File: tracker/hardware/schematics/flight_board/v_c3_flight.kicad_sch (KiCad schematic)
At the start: 20 parts, among them J1 Prog_Header, J2 Debug_Header, U1 ESP32-C3-WROOM-02, U2 LR2021F33, U3 MAX-M10S, U4 TPS7A02, U5 BMP280

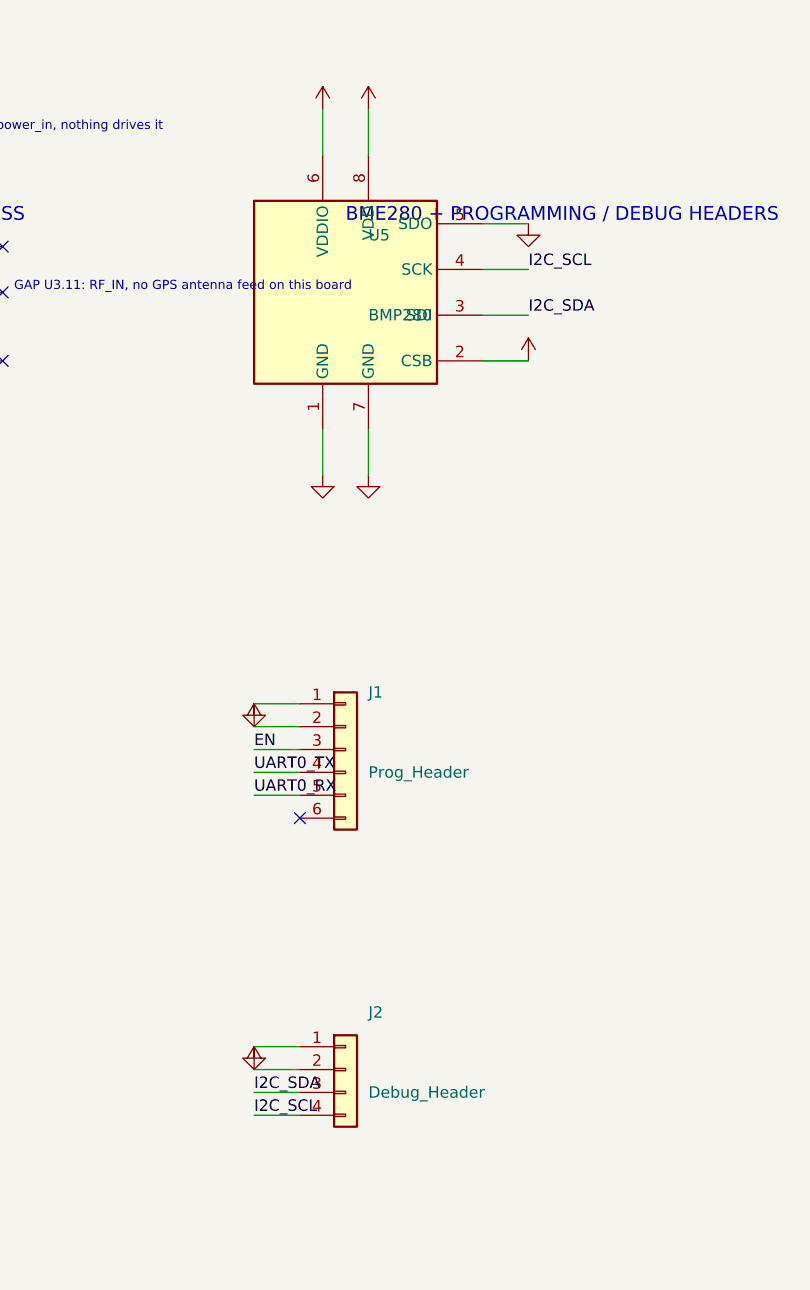
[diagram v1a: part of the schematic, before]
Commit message: M1: align MS5611 design-backing artifacts (BOM, netlist, generator, schematics)
- v8b BOM/position files now list U5 as MS5611 with Package_LGA:LGA-8_3x5mm_P1.25mm
- flight_board netlist, build script, and regenerated schematic now emit Sensor_Pressure:MS5611-01BA
- top-level v_c3_flight.kicad_sch U5 symbol/value/footprint updated to MS5611-01BA
- hub_schematic stale BMP280-only comment fixed

No active design source file still declares BMP280 as the populated part.
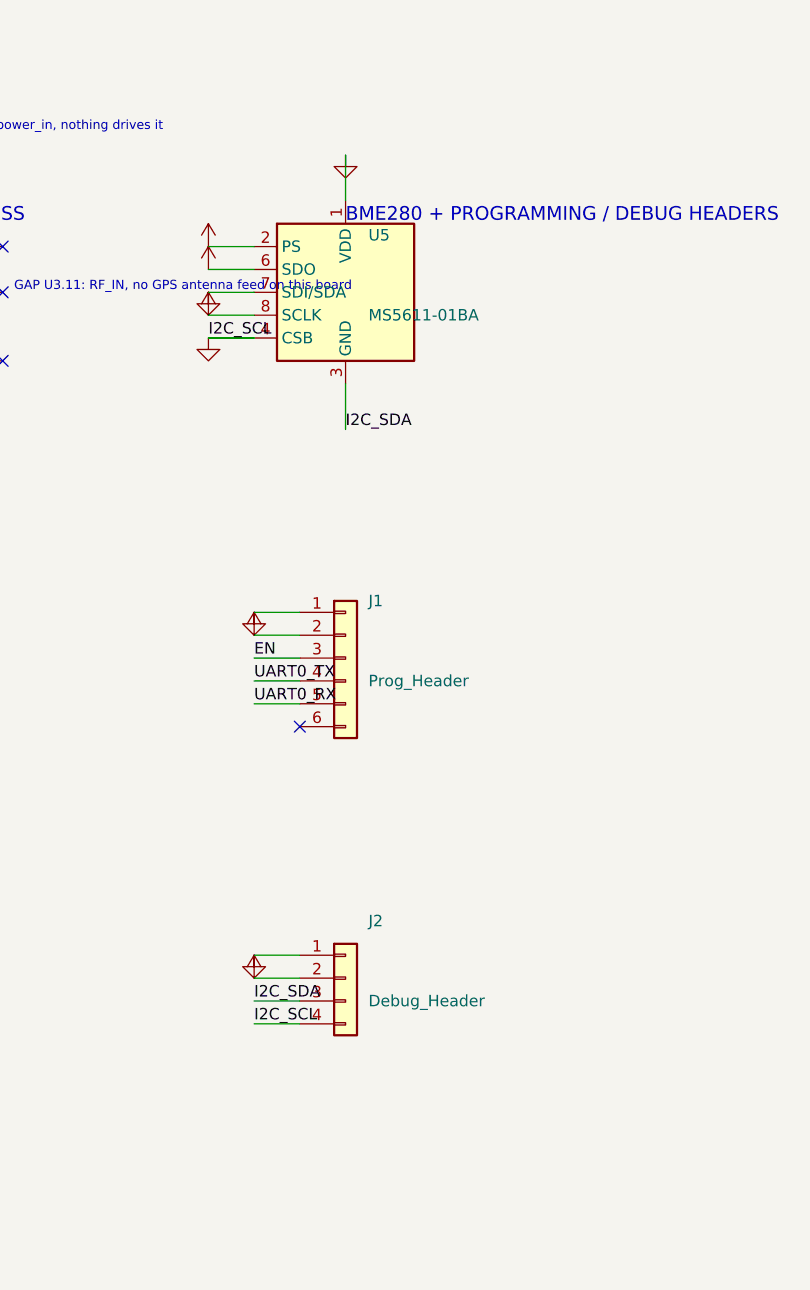
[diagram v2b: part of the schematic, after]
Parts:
- removed U5: BMP280, balloon_flight:Bosch_LGA-8_2.5x2.5mm_P0.65mm_ClockwisePinNumbering, symbol Sensor:BME280
- added U5: MS5611-01BA, Package_LGA:LGA-8_3x5mm_P1.25mm, symbol Sensor_Pressure:MS5611-01BA
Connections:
- net I2C_SCL is gone; now on net GND: J2.4 (Pin_4), U1.8 (IO9)
- net +3V3: now also U5.2 (PS), U5.6 (SDO), U5.8 (SCLK)
- net GND: now also U5.1 (VDD), U5.4 (CSB), U5.5 (CSB), U5.7 (SDI/SDA)
- net I2C_SDA: now also U5.3 (GND)

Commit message: fix(sch): sync flight schematic to v8i board of record (20→28 components)
Re-point build_flight_sch.py at the board of record
v8i_krt_gnss.kicad_pcb (28 footprints, 25 nets) instead of the stale
v_c3_flight_4layer_placed.kicad_pcb (20 footprints).  This brings the
drawing up to the board and closes the GNSS-path gap the drawing itself
documented.

Added 8 components present on the board but missing from the drawing:
  ANT2 (U.FL_GNSS), R_SER (0R), C_SH1/C_SH2 (DNP shunts), MNT1-4 (mounting holes)

GNSS antenna feed now wired:
  ANT2.1 -> GNSS_ANT -> R_SER -> GNSS_RF -> U3.11 (RF_IN)
  C_SH1 shunts GNSS_RF to GND; C_SH2 shunts GNSS_ANT to GND
  The 'no GPS antenna feed on this board' annotation is removed (U3.11
  now has a net, so the gap note no longer fires).

U2 updated to the 18-pin LoRa2021_Castellated footprint (Gen4 module)
with net-derived pin names; floating pads (10/13/16/17) left with
TODO(unverified) annotations (never tie a 2W PA module pin on a guess).

U3.9 (~RESET) and U3.6 (V_BCKP) are now tied to +3V3 by the board itself
(no longer floating).  U3.15 (VIO_SEL) and U3.18 (~SAFEBOOT) remain
floating with TODO(unverified) annotations — the u-blox MAX-M10S
integration manual was not sourced in time to apply the datasheet
tie-off.

U5 remains MS5611-01BA (value/footprint override preserved).  The symbol
is Sensor:BME280 (BMP280 pad numbering matching the board) with the
value/footprint overridden to MS5611-01BA / LGA-8_3x5mm_P1.25mm, fixing
a pin-numbering mismatch that caused ERC errors when mapped to the
Sensor_Pressure:MS5611-01BA symbol directly.

Verification: check_sch_gates.py ALL GATES PASS (0 ERC errors, 1
warning); kicad-cli sch export netlist emits 28 components; net/node
parity with the PCB verified both ways (24 nets, 98 nodes).
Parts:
- removed U5: MS5611-01BA, Package_LGA:LGA-8_3x5mm_P1.25mm, symbol Sensor_Pressure:MS5611-01BA
- added ANT2: U.FL_GNSS, balloon_flight:U.FL_Molex_MCRF_73412-0110_Vertical, symbol Connector:Conn_Coaxial
- added C_SH1, C_SH2: DNP, balloon_flight:C_0402_1005Metric, symbol Device:C
- added MNT1, MNT2, MNT3, MNT4: MountingHole, balloon_flight:MountingHole_2.2mm_M2, symbol Mechanical:MountingHole
- added R_SER: 0R, balloon_flight:R_0402_1005Metric, symbol Device:R
- added U5: MS5611-01BA, Package_LGA:LGA-8_3x5mm_P1.25mm, symbol Sensor:BME280
- U2: value LR2021F33 -> LoRa2021_Gen4; footprint balloon_flight:HOPERF_RFM9XW_SMD -> balloon_flight:LoRa2021_Castellated
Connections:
- net +3V3: now also U2.1 (VCC), U3.6 (V_BCKP), U3.9 (~{RESET}), U5.2 (CSB), U5.6 (VDDIO), U5.8 (VDD); no longer U2.13 (VCC)
- net GND: now also U2.11 (GND), U2.12 (GND), U2.18 (GND), U2.2 (GND), ANT2.2 (Ext), C_SH1.1, C_SH2.1, U5.1 (GND), U5.5 (SDO), U5.7 (GND); no longer J2.4 (Pin_4), U1.8 (IO9), U2.1 (GND), U2.10 (GND)
- net I2C_SDA: now also U5.3 (SDI)
- net LR_BUSY: now also U2.7 (BUSY); no longer U2.12 (BUSY)
- net LR_RST: now also U2.14 (RESET); no longer U2.6 (RESET)
- net SPI_MISO: now also U2.3 (MISO); no longer U2.2 (MISO)
- net SPI_MOSI: now also U2.4 (MOSI); no longer U2.3 (MOSI)
- net SPI_NSS: now also U2.6 (NSS); no longer U2.5 (NSS)
- net SPI_SCK: now also U2.5 (SCK); no longer U2.4 (SCK)
- net VCAP: now also U4.3 (EN)
- net GNSS_RF: now reaches U3.11 (RF_IN)
- net GNSS_RF: now also C_SH1.2, R_SER.2
- net LR_IRQ: now reaches U2.15 (DIO0)
- net LR_IRQ: now also U1.13 (IO18)
- removed net LR_DIO0: U1.13 (IO18), U2.14 (DIO0)
- new net GNSS_ANT: ANT2.1 (In), C_SH2.2, R_SER.1
- new net I2C_SCL: J2.4 (Pin_4), U1.8 (IO9), U5.4 (SCK)
- no-connect marks 18 -> 14
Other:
- note added: "BALLOON C3 FLIGHT BOARD - netlist mirror of v8i_krt_gnss.kicad_pcb"
- note added: "GAP U2.10: TODO(unverified): LoRa2021 Gen4 pad 10 function / termination"
- note added: "GAP U2.13: TODO(unverified): LoRa2021 Gen4 pad 13 function / termination"
- note added: "GAP U2.16: TODO(unverified): LoRa2021 Gen4 pad 16 function / termination"
- note added: "GAP U2.17: TODO(unverified): LoRa2021 Gen4 pad 17 function / termination"
- note added: "GAP U3.15: TODO(unverified): MAX-M10S VIO_SEL tie-off required"
- note added: "GAP U3.18: TODO(unverified): MAX-M10S ~SAFEBOOT inactive level tie-off required"
- note added: "GAP U4.4: TODO(unverified): TPS7A02 pin 4 function / tie-off"
- note added: "LR2021F33 RADIO (18-pin castellated)"
- note added: "MAX-M10S GNSS + ANT2 FEED"
- note added: "MOUNTING HOLES"
- note added: "MS5611 + PROGRAMMING / DEBUG HEADERS"
- note added: "PCB sha256 638de56387721460... - schematic is DERIVED, the PCB is the source of truth (ADR-028)"
- note removed: "BALLOON C3 FLIGHT BOARD - netlist mirror of v_c3_flight_4layer_placed.kicad_pcb"
- note removed: "BME280 + PROGRAMMING / DEBUG HEADERS"
- note removed: "GAP U2.11: probable GND tab left floating"
- note removed: "GAP U2.15: unmodelled RF module I/O"
- note removed: "GAP U2.16: probable GND tab left floating"
- note removed: "GAP U2.7: unmodelled RF module I/O"
- note removed: "GAP U3.11: RF_IN, no GPS antenna feed on this board"
- note removed: "GAP U3.15: VIO_SEL floating"
- note removed: "GAP U3.18: ~SAFEBOOT floating"
- note removed: "GAP U3.6: V_BCKP power_in, nothing drives it"
- note removed: "GAP U3.9: ~RESET floating"
- note removed: "GAP U4.3: EN floating, rail never explicitly enabled"
- note removed: "GAP U4.4: OUT/NC contradiction between in-repo sources"
- note removed: "LR2021F33 RADIO (16-pad footprint)"
- note removed: "MAX-M10S GNSS"
- note removed: "PCB sha256 f3cf0143e7deff99... - schematic is DERIVED, the PCB is the source of truth (ADR-028)"
